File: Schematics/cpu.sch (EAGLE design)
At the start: 44 parts, among them IC2 LM555N, IC22 74154N, IC3 LM555N, IC4 7400N, IC5 74LS32N, IC6 ATMEGA328-20P, U1 74HC245N,652, U2 74HC245N,652, U3 74HC245N,652, U4 74HC04N,652

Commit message: removed arduino, added io interrupt, finished io read
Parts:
- removed I/O10, I/O11, I/O12, I/O13, I/O14, I/O15, I/O16, I/O2, I/O3, I/O4, I/O5, I/O6, I/O7, I/O8, I/O9: 74AS573N, 74xx-us:74AS573N
- removed IC22: 74154N, 74xx-us:74154N
- added I/O17, I/O18, I/O19, I/O20, I/O21, I/O22, I/O23, I/O24, I/O25, I/O26, I/O27, I/O28, I/O29, I/O30, I/O31, I/O32: 74AS573N, 74xx-us:74AS573N
- added IC7: 74LS32N, 74xx-us:74LS32N
- added IC8, IC9: 74154N, 74xx-us:74154N
- IC6: value ATMEGA328-20P -> 74LS32N; device atmega328:ATMEGA328-20P -> 74xx-us:74LS32N
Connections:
- removed net N$40: I/O3A.OC, IC22A.2
- removed net N$41: I/O4A.OC, IC22A.3
- removed net N$42: I/O5A.OC, IC22A.4
- removed net N$43: I/O6A.OC, IC22A.5
- removed net N$44: I/O7A.OC, IC22A.6
- removed net N$45: I/O8A.OC, IC22A.7
- removed net N$46: I/O9A.OC, IC22A.8
- removed net N$47: I/O10A.OC, IC22A.9
- removed net N$48: I/O11A.OC, IC22A.10
- removed net N$49: I/O12A.OC, IC22A.11
- removed net N$50: I/O13A.OC, IC22A.12
- removed net N$51: I/O15A.OC, IC22A.13
- removed net N$52: I/O16A.OC, IC22A.14
- removed net N$53: IC6.(PCI18/INT0)PD2
- removed net N$54: IC6.(PCI19/INT1/OC2B)PD3
- removed net N$55: IC6.(PCI12/ADC4/SDA)PC4
- removed net N$56: IC6.(PCI13/ADC5/SCL)PC5
- removed net N$57: IC6.(PCI16/RXD)PD0
- removed net N$58: IC6.(PCI17/TXD)PD1
- removed net N$59: IC6.(PCI5/SCK)PB5
- removed net N$60: IC6.(PCI4/MISO)PB4
- removed net N$61: IC6.(PCI3/MOSI/OC2A)PB3
- removed net N$62: IC6.(PCI2/SS/OC1B)PB2
- removed net N$63: IC6.(PCI21/T1/OC0B)PD5
- new net IOADD0: IC9A.A
- new net IOADD1: IC9A.B
- new net IOADD2: IC9A.C
- new net IOADD3: IC9A.D
- new net IO_READ_CPULS0: I/O17A.OC, IC8A.0
- new net IO_READ_CPULS1: I/O18A.OC, IC8A.1
- new net IO_READ_CPULS10: I/O27A.OC, IC8A.10
- new net IO_READ_CPULS11: I/O28A.OC, IC8A.11
- new net IO_READ_CPULS12: I/O29A.OC, IC8A.12
- new net IO_READ_CPULS13: I/O30A.OC, IC8A.13
- new net IO_READ_CPULS14: I/O31A.OC, IC8A.14
- new net IO_READ_CPULS15: I/O32A.OC, IC8A.15
- new net IO_READ_CPULS2: I/O19A.OC, IC8A.2
- new net IO_READ_CPULS3: I/O20A.OC, IC8A.3
- new net IO_READ_CPULS4: I/O21A.OC, IC8A.4
- new net IO_READ_CPULS5: I/O22A.OC, IC8A.5
- new net IO_READ_CPULS6: I/O23A.OC, IC8A.6
- new net IO_READ_CPULS7: I/O24A.OC, IC8A.7
- new net IO_READ_CPULS8: I/O25A.OC, IC8A.8
- new net IO_READ_CPULS9: I/O26A.OC, IC8A.9
- new net IO_READ_IOLS0: I/O17A.C, IC9A.0
- new net IO_READ_IOLS1: I/O18A.C, IC9A.1
- new net IO_READ_IOLS10: I/O27A.C, IC9A.10
- new net IO_READ_IOLS11: I/O28A.C, IC9A.11
- new net IO_READ_IOLS12: I/O29A.C, IC9A.12
- new net IO_READ_IOLS13: I/O30A.C, IC9A.13
- new net IO_READ_IOLS14: I/O31A.C, IC9A.14
- new net IO_READ_IOLS15: I/O32A.C, IC9A.15
- new net IO_READ_IOLS2: I/O19A.C, IC9A.2
- new net IO_READ_IOLS3: I/O20A.C, IC9A.3
- new net IO_READ_IOLS4: I/O21A.C, IC9A.4
- new net IO_READ_IOLS5: I/O22A.C, IC9A.5
- new net IO_READ_IOLS6: I/O23A.C, IC9A.6
- new net IO_READ_IOLS7: I/O24A.C, IC9A.7
- new net IO_READ_IOLS8: I/O25A.C, IC9A.8
- new net IO_READ_IOLS9: I/O26A.C, IC9A.9
- new net LATCH_EN: IC9A.G1, IC9A.G2
- new net M1: IC7D.I1
- net ADD0: now also IC8A.A; no longer IC22A.A
- net ADD1: now also IC8A.B; no longer IC22A.B
- net ADD2: now also IC8A.C; no longer IC22A.C
- net ADD3: now also IC8A.D; no longer IC22A.D
- net DAT0: now also I/O17A.1Q, I/O18A.1Q, I/O19A.1Q, I/O20A.1Q, I/O21A.1Q, I/O22A.1Q, I/O23A.1Q, I/O24A.1Q, I/O25A.1Q, I/O26A.1Q, I/O27A.1Q, I/O28A.1Q, I/O29A.1Q, I/O30A.1Q, I/O31A.1Q, I/O32A.1Q; no longer I/O10A.1Q, I/O11A.1Q, I/O12A.1Q, I/O13A.1Q, I/O14A.1Q, I/O15A.1Q, I/O16A.1Q, I/O2A.1Q, I/O3A.1Q, I/O4A.1Q, I/O5A.1Q, I/O6A.1Q, I/O7A.1Q, I/O8A.1Q, I/O9A.1Q
- net DAT1: now also I/O17A.2Q, I/O18A.2Q, I/O19A.2Q, I/O20A.2Q, I/O21A.2Q, I/O22A.2Q, I/O23A.2Q, I/O24A.2Q, I/O25A.2Q, I/O26A.2Q, I/O27A.2Q, I/O28A.2Q, I/O29A.2Q, I/O30A.2Q, I/O31A.2Q, I/O32A.2Q; no longer I/O10A.2Q, I/O11A.2Q, I/O12A.2Q, I/O13A.2Q, I/O14A.2Q, I/O15A.2Q, I/O16A.2Q, I/O2A.2Q, I/O3A.2Q, I/O4A.2Q, I/O5A.2Q, I/O6A.2Q, I/O7A.2Q, I/O8A.2Q, I/O9A.2Q
- net DAT2: now also I/O17A.3Q, I/O18A.3Q, I/O19A.3Q, I/O20A.3Q, I/O21A.3Q, I/O22A.3Q, I/O23A.3Q, I/O24A.3Q, I/O25A.3Q, I/O26A.3Q, I/O27A.3Q, I/O28A.3Q, I/O29A.3Q, I/O30A.3Q, I/O31A.3Q, I/O32A.3Q; no longer I/O10A.3Q, I/O11A.3Q, I/O12A.3Q, I/O13A.3Q, I/O14A.3Q, I/O15A.3Q, I/O16A.3Q, I/O2A.3Q, I/O3A.3Q, I/O4A.3Q, I/O5A.3Q, I/O6A.3Q, I/O7A.3Q, I/O8A.3Q, I/O9A.3Q
- net DAT3: now also I/O17A.4Q, I/O18A.4Q, I/O19A.4Q, I/O20A.4Q, I/O21A.4Q, I/O22A.4Q, I/O23A.4Q, I/O24A.4Q, I/O25A.4Q, I/O26A.4Q, I/O27A.4Q, I/O28A.4Q, I/O29A.4Q, I/O30A.4Q, I/O31A.4Q, I/O32A.4Q; no longer I/O10A.4Q, I/O11A.4Q, I/O12A.4Q, I/O13A.4Q, I/O14A.4Q, I/O15A.4Q, I/O16A.4Q, I/O2A.4Q, I/O3A.4Q, I/O4A.4Q, I/O5A.4Q, I/O6A.4Q, I/O7A.4Q, I/O8A.4Q, I/O9A.4Q
- net DAT4: now also I/O17A.5Q, I/O18A.5Q, I/O19A.5Q, I/O20A.5Q, I/O21A.5Q, I/O22A.5Q, I/O23A.5Q, I/O24A.5Q, I/O25A.5Q, I/O26A.5Q, I/O27A.5Q, I/O28A.5Q, I/O29A.5Q, I/O30A.5Q, I/O31A.5Q, I/O32A.5Q; no longer I/O10A.5Q, I/O11A.5Q, I/O12A.5Q, I/O13A.5Q, I/O14A.5Q, I/O15A.5Q, I/O16A.5Q, I/O2A.5Q, I/O3A.5Q, I/O4A.5Q, I/O5A.5Q, I/O6A.5Q, I/O7A.5Q, I/O8A.5Q, I/O9A.5Q
- net DAT5: now also I/O17A.6Q, I/O18A.6Q, I/O19A.6Q, I/O20A.6Q, I/O21A.6Q, I/O22A.6Q, I/O23A.6Q, I/O24A.6Q, I/O25A.6Q, I/O26A.6Q, I/O27A.6Q, I/O28A.6Q, I/O29A.6Q, I/O30A.6Q, I/O31A.6Q, I/O32A.6Q; no longer I/O10A.6Q, I/O11A.6Q, I/O12A.6Q, I/O13A.6Q, I/O14A.6Q, I/O15A.6Q, I/O16A.6Q, I/O2A.6Q, I/O3A.6Q, I/O4A.6Q, I/O5A.6Q, I/O6A.6Q, I/O7A.6Q, I/O8A.6Q, I/O9A.6Q
- net DAT6: now also I/O17A.7Q, I/O18A.7Q, I/O19A.7Q, I/O20A.7Q, I/O21A.7Q, I/O22A.7Q, I/O23A.7Q, I/O24A.7Q, I/O25A.7Q, I/O26A.7Q, I/O27A.7Q, I/O28A.7Q, I/O29A.7Q, I/O30A.7Q, I/O31A.7Q, I/O32A.7Q; no longer I/O10A.7Q, I/O11A.7Q, I/O12A.7Q, I/O13A.7Q, I/O14A.7Q, I/O15A.7Q, I/O16A.7Q, I/O2A.7Q, I/O3A.7Q, I/O4A.7Q, I/O5A.7Q, I/O6A.7Q, I/O7A.7Q, I/O8A.7Q, I/O9A.7Q
- net DAT7: now also I/O17A.8Q, I/O18A.8Q, I/O19A.8Q, I/O20A.8Q, I/O21A.8Q, I/O22A.8Q, I/O23A.8Q, I/O24A.8Q, I/O25A.8Q, I/O26A.8Q, I/O27A.8Q, I/O28A.8Q, I/O29A.8Q, I/O30A.8Q, I/O31A.8Q, I/O32A.8Q; no longer I/O10A.8Q, I/O11A.8Q, I/O12A.8Q, I/O13A.8Q, I/O14A.8Q, I/O15A.8Q, I/O16A.8Q, I/O2A.8Q, I/O3A.8Q, I/O4A.8Q, I/O5A.8Q, I/O6A.8Q, I/O7A.8Q, I/O8A.8Q, I/O9A.8Q
- net I/ODAT0: now also I/O17A.1D, I/O19A.1D, I/O20A.1D, I/O21A.1D, I/O22A.1D, I/O23A.1D, I/O24A.1D, I/O25A.1D, I/O26A.1D, I/O27A.1D, I/O28A.1D, I/O29A.1D, I/O30A.1D, I/O31A.1D, I/O32A.1D; no longer I/O10A.1D, I/O11A.1D, I/O12A.1D, I/O13A.1D, I/O14A.1D, I/O15A.1D, I/O16A.1D, I/O3A.1D, I/O4A.1D, I/O5A.1D, I/O6A.1D, I/O7A.1D, I/O8A.1D, I/O9A.1D
- net I/ODAT1: now also I/O17A.2D, I/O19A.2D, I/O20A.2D, I/O21A.2D, I/O22A.2D, I/O23A.2D, I/O24A.2D, I/O25A.2D, I/O26A.2D, I/O27A.2D, I/O28A.2D, I/O29A.2D, I/O30A.2D, I/O31A.2D, I/O32A.2D; no longer I/O10A.2D, I/O11A.2D, I/O12A.2D, I/O13A.2D, I/O14A.2D, I/O15A.2D, I/O16A.2D, I/O3A.2D, I/O4A.2D, I/O5A.2D, I/O6A.2D, I/O7A.2D, I/O8A.2D, I/O9A.2D
- net I/ODAT2: now also I/O17A.3D, I/O19A.3D, I/O20A.3D, I/O21A.3D, I/O22A.3D, I/O23A.3D, I/O24A.3D, I/O25A.3D, I/O26A.3D, I/O27A.3D, I/O28A.3D, I/O29A.3D, I/O30A.3D, I/O31A.3D, I/O32A.3D; no longer I/O10A.3D, I/O11A.3D, I/O12A.3D, I/O13A.3D, I/O14A.3D, I/O15A.3D, I/O16A.3D, I/O3A.3D, I/O4A.3D, I/O5A.3D, I/O6A.3D, I/O7A.3D, I/O8A.3D, I/O9A.3D
- net I/ODAT3: now also I/O17A.4D, I/O19A.4D, I/O20A.4D, I/O21A.4D, I/O22A.4D, I/O23A.4D, I/O24A.4D, I/O25A.4D, I/O26A.4D, I/O27A.4D, I/O28A.4D, I/O29A.4D, I/O30A.4D, I/O31A.4D, I/O32A.4D; no longer I/O10A.4D, I/O11A.4D, I/O12A.4D, I/O13A.4D, I/O14A.4D, I/O15A.4D, I/O16A.4D, I/O3A.4D, I/O4A.4D, I/O5A.4D, I/O6A.4D, I/O7A.4D, I/O8A.4D, I/O9A.4D
- net I/ODAT4: now also I/O17A.5D, I/O19A.5D, I/O20A.5D, I/O21A.5D, I/O22A.5D, I/O23A.5D, I/O24A.5D, I/O25A.5D, I/O26A.5D, I/O27A.5D, I/O28A.5D, I/O29A.5D, I/O30A.5D, I/O31A.5D, I/O32A.5D; no longer I/O10A.5D, I/O11A.5D, I/O12A.5D, I/O13A.5D, I/O14A.5D, I/O15A.5D, I/O16A.5D, I/O3A.5D, I/O4A.5D, I/O5A.5D, I/O6A.5D, I/O7A.5D, I/O8A.5D, I/O9A.5D
- net I/ODAT5: now also I/O17A.6D, I/O19A.6D, I/O20A.6D, I/O21A.6D, I/O22A.6D, I/O23A.6D, I/O24A.6D, I/O25A.6D, I/O26A.6D, I/O27A.6D, I/O28A.6D, I/O29A.6D, I/O30A.6D, I/O31A.6D, I/O32A.6D; no longer I/O10A.6D, I/O11A.6D, I/O12A.6D, I/O13A.6D, I/O14A.6D, I/O15A.6D, I/O16A.6D, I/O3A.6D, I/O4A.6D, I/O5A.6D, I/O6A.6D, I/O7A.6D, I/O8A.6D, I/O9A.6D
- net I/ODAT6: now also I/O17A.7D, I/O19A.7D, I/O20A.7D, I/O21A.7D, I/O22A.7D, I/O23A.7D, I/O24A.7D, I/O25A.7D, I/O26A.7D, I/O27A.7D, I/O28A.7D, I/O29A.7D, I/O30A.7D, I/O31A.7D, I/O32A.7D; no longer I/O10A.7D, I/O11A.7D, I/O12A.7D, I/O13A.7D, I/O14A.7D, I/O15A.7D, I/O16A.7D, I/O3A.7D, I/O4A.7D, I/O5A.7D, I/O6A.7D, I/O7A.7D, I/O8A.7D, I/O9A.7D
- net I/ODAT7: now also I/O17A.8D, I/O19A.8D, I/O20A.8D, I/O21A.8D, I/O22A.8D, I/O23A.8D, I/O24A.8D, I/O25A.8D, I/O26A.8D, I/O27A.8D, I/O28A.8D, I/O29A.8D, I/O30A.8D, I/O31A.8D, I/O32A.8D; no longer I/O10A.8D, I/O11A.8D, I/O12A.8D, I/O13A.8D, I/O14A.8D, I/O15A.8D, I/O16A.8D, I/O3A.8D, I/O4A.8D, I/O5A.8D, I/O6A.8D, I/O7A.8D, I/O8A.8D, I/O9A.8D
- net IORD: now also IC6D.O, IC8A.G1, IC8A.G2; no longer IC22A.G1, IC22A.G2, IC5D.O
- net IORQ: now also IC6D.I1, IC7D.I0; no longer IC5D.I1
- net N$38: now also IC7D.O; no longer IC22A.0
- net N$39: now also I/O1A.C; no longer I/O2A.OC, IC22A.1
- net RD: now also IC6D.I0; no longer IC5D.I0
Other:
- note added: "IO Inturrupt"
- note added: "IO Read"

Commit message: finished io decoding, started to change the latch part used to a better library one
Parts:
- removed I/O1: 74AS573N, 74xx-us:74AS573N
- added IC10: 74LS32N, 74xx-us:74LS32N
- added U5, U6, U7: 74HC373N,652, NXP_By_element14_Batch_1:74HC373N,652
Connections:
- new net 5V: U7.VCC
- new net HALT: IC1.HALT
- new net IORW: IC10D.I0
- new net IO_ADD0: U5.D0
- new net IO_ADD1: U5.D1
- new net IO_ADD2: U5.D2
- new net IO_ADD3: U5.D3
- new net IO_ADD4: U5.D4
- new net IO_ADD5: U5.D5
- new net IO_ADD6: U5.D6
- new net IO_ADD7: U5.D7
- new net IO_INT: U7.LE
- new net N$40: U5.~OE, U6.~OE
- new net RFSH: IC1.RFSH
- new net WAIT: IC1.WAIT
- net ADD0: now also U5.Q0
- net ADD1: now also U5.Q1
- net ADD2: now also U5.Q2
- net ADD3: now also U5.Q3
- net ADD4: now also U5.Q4
- net ADD5: now also U5.Q5
- net ADD6: now also U5.Q6
- net ADD7: now also U5.Q7
- net DAT0: now also U6.Q0, U7.Q0; no longer I/O1A.1Q
- net DAT1: now also U6.Q1, U7.Q1; no longer I/O1A.2Q
- net DAT2: now also U6.Q2, U7.Q2; no longer I/O1A.3Q
- net DAT3: now also U6.Q3, U7.Q3; no longer I/O1A.4Q
- net DAT4: now also U6.Q4, U7.Q4; no longer I/O1A.5Q
- net DAT5: now also U6.Q5, U7.Q5; no longer I/O1A.6Q
- net DAT6: now also U6.Q6, U7.Q6; no longer I/O1A.7Q
- net DAT7: now also U6.Q7, U7.Q7; no longer I/O1A.8Q
- net GND: now also U5.GND, U6.GND, U7.GND
- net I/ODAT0: now also U6.D0, U7.D0; no longer I/O1A.1D
- net I/ODAT1: now also U6.D1, U7.D1; no longer I/O1A.2D
- net I/ODAT2: now also U6.D2, U7.D2; no longer I/O1A.3D
- net I/ODAT3: now also U6.D3, U7.D3; no longer I/O1A.4D
- net I/ODAT4: now also U6.D4, U7.D4; no longer I/O1A.5D
- net I/ODAT5: now also U6.D5, U7.D5; no longer I/O1A.6D
- net I/ODAT6: now also U6.D6, U7.D6; no longer I/O1A.7D
- net I/ODAT7: now also U6.D7, U7.D7; no longer I/O1A.8D
- net N$38: now also U7.~OE; no longer I/O1A.OC
- net N$39: now also IC10D.O, U5.LE, U6.LE; no longer I/O1A.C
- net VCC: now also U5.VCC, U6.VCC
- net WR: now also IC10D.I1
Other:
- note added: "IO Port Write"
- note added: "NOTE: Only utilizing 8 ports of IO read, but all 256 ports of IO write. Maybe the IO controller will do sound as well?"
- moved on the sheet: IC7D

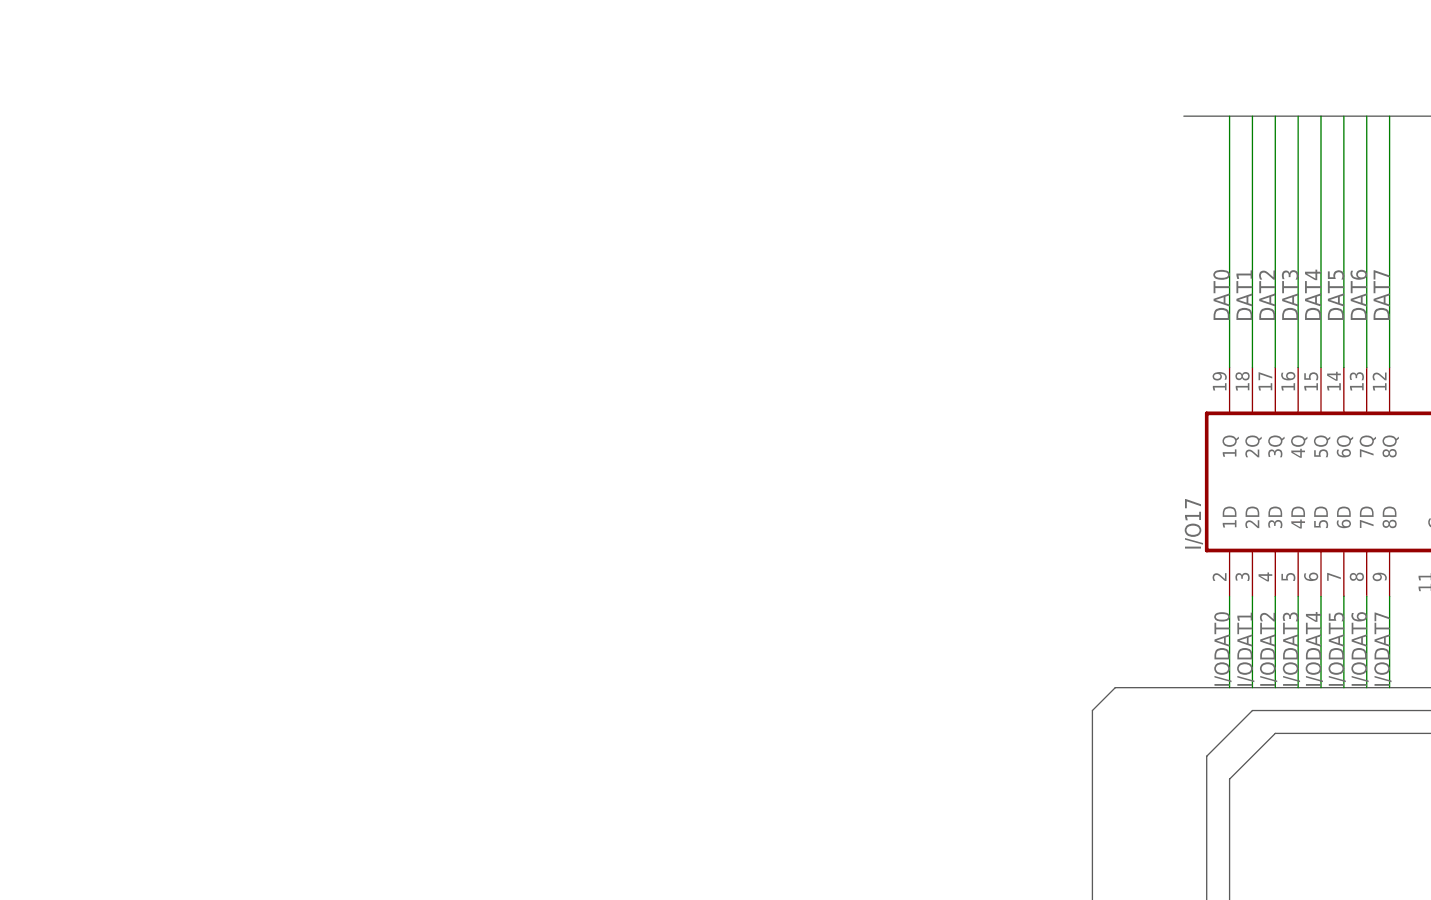
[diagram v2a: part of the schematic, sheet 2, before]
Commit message: figured out 40 pin mapping, started selecting microcontroller
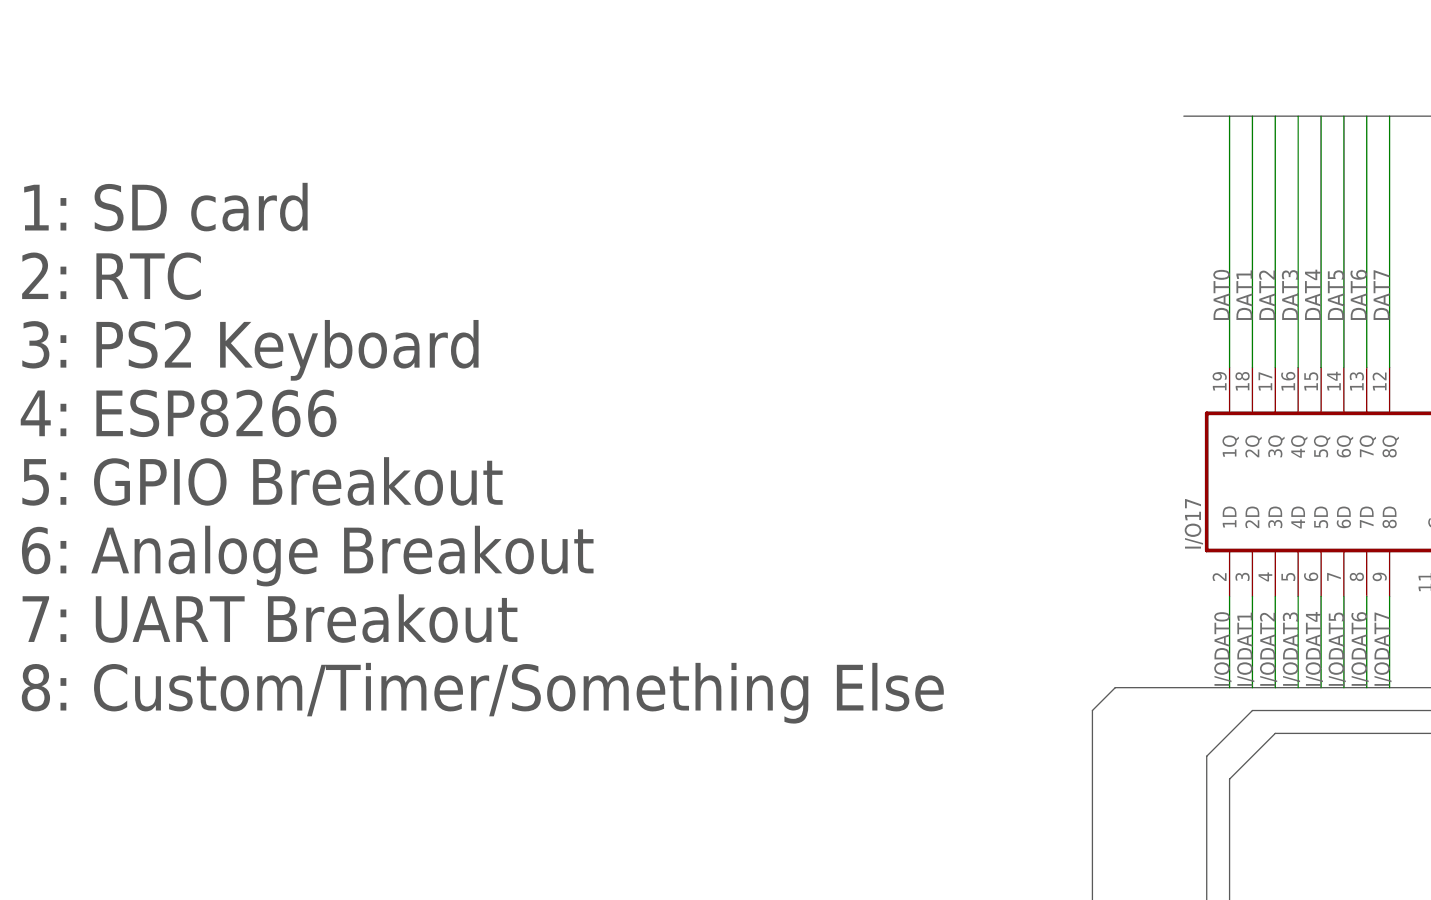
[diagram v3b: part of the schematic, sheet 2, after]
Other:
- note added: "1: SD card 2: RTC 3: PS2 Keyboard 4: ESP8266 5: GPIO Breakout 6: Analoge Breakout 7: UART Breakout 8: Custom/Timer/Something Else"
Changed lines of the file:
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@@
 all 256 ports of IO write. Maybe the IO controller
 will do sound as well?</text>
+<text x="-462.28" y="93.98" size="5.08" layer="97">1: SD card
+2: RTC
+3: PS2 Keyboard
+4: ESP8266
+5: GPIO Breakout
+6: Analoge Breakout
+7: UART Breakout
+8: Custom/Timer/Something Else
+</text>
 </plain>
 <instances>

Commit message: changed latches
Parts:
- removed I/O17, I/O18, I/O19, I/O20, I/O21, I/O22, I/O23, I/O24, I/O25, I/O26, I/O27, I/O28, I/O29, I/O30, I/O31, I/O32: 74AS573N, 74xx-us:74AS573N
- added U10, U11, U12, U13, U14, U15, U8, U9: 74HC373N,652, NXP_By_element14_Batch_1:74HC373N,652
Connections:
- net DAT0: now also U10.Q0, U11.Q0, U12.Q0, U13.Q0, U14.Q0, U15.Q0, U8.Q0, U9.Q0; no longer I/O17A.1Q, I/O18A.1Q, I/O19A.1Q, I/O20A.1Q, I/O21A.1Q, I/O22A.1Q, I/O23A.1Q, I/O24A.1Q, I/O25A.1Q, I/O26A.1Q, I/O27A.1Q, I/O28A.1Q, I/O29A.1Q, I/O30A.1Q, I/O31A.1Q, I/O32A.1Q
- net DAT1: now also U10.Q1, U11.Q1, U12.Q1, U13.Q1, U14.Q1, U15.Q1, U8.Q1, U9.Q1; no longer I/O17A.2Q, I/O18A.2Q, I/O19A.2Q, I/O20A.2Q, I/O21A.2Q, I/O22A.2Q, I/O23A.2Q, I/O24A.2Q, I/O25A.2Q, I/O26A.2Q, I/O27A.2Q, I/O28A.2Q, I/O29A.2Q, I/O30A.2Q, I/O31A.2Q, I/O32A.2Q
- net DAT2: now also U10.Q2, U11.Q2, U12.Q2, U13.Q2, U14.Q2, U15.Q2, U8.Q2, U9.Q2; no longer I/O17A.3Q, I/O18A.3Q, I/O19A.3Q, I/O20A.3Q, I/O21A.3Q, I/O22A.3Q, I/O23A.3Q, I/O24A.3Q, I/O25A.3Q, I/O26A.3Q, I/O27A.3Q, I/O28A.3Q, I/O29A.3Q, I/O30A.3Q, I/O31A.3Q, I/O32A.3Q
- net DAT3: now also U10.Q3, U11.Q3, U12.Q3, U13.Q3, U14.Q3, U15.Q3, U8.Q3, U9.Q3; no longer I/O17A.4Q, I/O18A.4Q, I/O19A.4Q, I/O20A.4Q, I/O21A.4Q, I/O22A.4Q, I/O23A.4Q, I/O24A.4Q, I/O25A.4Q, I/O26A.4Q, I/O27A.4Q, I/O28A.4Q, I/O29A.4Q, I/O30A.4Q, I/O31A.4Q, I/O32A.4Q
- net DAT4: now also U10.Q4, U11.Q4, U12.Q4, U13.Q4, U14.Q4, U15.Q4, U8.Q4, U9.Q4; no longer I/O17A.5Q, I/O18A.5Q, I/O19A.5Q, I/O20A.5Q, I/O21A.5Q, I/O22A.5Q, I/O23A.5Q, I/O24A.5Q, I/O25A.5Q, I/O26A.5Q, I/O27A.5Q, I/O28A.5Q, I/O29A.5Q, I/O30A.5Q, I/O31A.5Q, I/O32A.5Q
- net DAT5: now also U10.Q5, U11.Q5, U12.Q5, U13.Q5, U14.Q5, U15.Q5, U8.Q5, U9.Q5; no longer I/O17A.6Q, I/O18A.6Q, I/O19A.6Q, I/O20A.6Q, I/O21A.6Q, I/O22A.6Q, I/O23A.6Q, I/O24A.6Q, I/O25A.6Q, I/O26A.6Q, I/O27A.6Q, I/O28A.6Q, I/O29A.6Q, I/O30A.6Q, I/O31A.6Q, I/O32A.6Q
- net DAT6: now also U10.Q6, U11.Q6, U12.Q6, U13.Q6, U14.Q6, U15.Q6, U8.Q6, U9.Q6; no longer I/O17A.7Q, I/O18A.7Q, I/O19A.7Q, I/O20A.7Q, I/O21A.7Q, I/O22A.7Q, I/O23A.7Q, I/O24A.7Q, I/O25A.7Q, I/O26A.7Q, I/O27A.7Q, I/O28A.7Q, I/O29A.7Q, I/O30A.7Q, I/O31A.7Q, I/O32A.7Q
- net DAT7: now also U10.Q7, U11.Q7, U12.Q7, U13.Q7, U14.Q7, U15.Q7, U8.Q7, U9.Q7; no longer I/O17A.8Q, I/O18A.8Q, I/O19A.8Q, I/O20A.8Q, I/O21A.8Q, I/O22A.8Q, I/O23A.8Q, I/O24A.8Q, I/O25A.8Q, I/O26A.8Q, I/O27A.8Q, I/O28A.8Q, I/O29A.8Q, I/O30A.8Q, I/O31A.8Q, I/O32A.8Q
- net GND: now also U8.GND
- net I/ODAT0: now also U10.D0, U11.D0, U12.D0, U13.D0, U14.D0, U15.D0, U8.D0, U9.D0; no longer I/O17A.1D, I/O19A.1D, I/O20A.1D, I/O21A.1D, I/O22A.1D, I/O23A.1D, I/O24A.1D, I/O25A.1D, I/O26A.1D, I/O27A.1D, I/O28A.1D, I/O29A.1D, I/O30A.1D, I/O31A.1D, I/O32A.1D
- net I/ODAT1: now also U10.D1, U11.D1, U12.D1, U13.D1, U14.D1, U15.D1, U8.D1, U9.D1; no longer I/O17A.2D, I/O19A.2D, I/O20A.2D, I/O21A.2D, I/O22A.2D, I/O23A.2D, I/O24A.2D, I/O25A.2D, I/O26A.2D, I/O27A.2D, I/O28A.2D, I/O29A.2D, I/O30A.2D, I/O31A.2D, I/O32A.2D
- net I/ODAT2: now also U10.D2, U11.D2, U12.D2, U13.D2, U14.D2, U15.D2, U8.D2, U9.D2; no longer I/O17A.3D, I/O19A.3D, I/O20A.3D, I/O21A.3D, I/O22A.3D, I/O23A.3D, I/O24A.3D, I/O25A.3D, I/O26A.3D, I/O27A.3D, I/O28A.3D, I/O29A.3D, I/O30A.3D, I/O31A.3D, I/O32A.3D
- net I/ODAT3: now also U10.D3, U11.D3, U12.D3, U13.D3, U14.D3, U15.D3, U8.D3, U9.D3; no longer I/O17A.4D, I/O19A.4D, I/O20A.4D, I/O21A.4D, I/O22A.4D, I/O23A.4D, I/O24A.4D, I/O25A.4D, I/O26A.4D, I/O27A.4D, I/O28A.4D, I/O29A.4D, I/O30A.4D, I/O31A.4D, I/O32A.4D
- net I/ODAT4: now also U10.D4, U11.D4, U12.D4, U13.D4, U14.D4, U15.D4, U8.D4, U9.D4; no longer I/O17A.5D, I/O19A.5D, I/O20A.5D, I/O21A.5D, I/O22A.5D, I/O23A.5D, I/O24A.5D, I/O25A.5D, I/O26A.5D, I/O27A.5D, I/O28A.5D, I/O29A.5D, I/O30A.5D, I/O31A.5D, I/O32A.5D
- net I/ODAT5: now also U10.D5, U11.D5, U12.D5, U13.D5, U14.D5, U15.D5, U8.D5, U9.D5; no longer I/O17A.6D, I/O19A.6D, I/O20A.6D, I/O21A.6D, I/O22A.6D, I/O23A.6D, I/O24A.6D, I/O25A.6D, I/O26A.6D, I/O27A.6D, I/O28A.6D, I/O29A.6D, I/O30A.6D, I/O31A.6D, I/O32A.6D
- net I/ODAT6: now also U10.D6, U11.D6, U12.D6, U13.D6, U14.D6, U15.D6, U8.D6, U9.D6; no longer I/O17A.7D, I/O19A.7D, I/O20A.7D, I/O21A.7D, I/O22A.7D, I/O23A.7D, I/O24A.7D, I/O25A.7D, I/O26A.7D, I/O27A.7D, I/O28A.7D, I/O29A.7D, I/O30A.7D, I/O31A.7D, I/O32A.7D
- net I/ODAT7: now also U10.D7, U11.D7, U12.D7, U13.D7, U14.D7, U15.D7, U8.D7, U9.D7; no longer I/O17A.8D, I/O19A.8D, I/O20A.8D, I/O21A.8D, I/O22A.8D, I/O23A.8D, I/O24A.8D, I/O25A.8D, I/O26A.8D, I/O27A.8D, I/O28A.8D, I/O29A.8D, I/O30A.8D, I/O31A.8D, I/O32A.8D
- net IO_READ_CPULS0: now also U8.~OE; no longer I/O17A.OC
- net IO_READ_CPULS1: now also U9.~OE; no longer I/O18A.OC
- net IO_READ_CPULS10: no longer I/O27A.OC
- net IO_READ_CPULS11: no longer I/O28A.OC
- net IO_READ_CPULS12: no longer I/O29A.OC
- net IO_READ_CPULS13: no longer I/O30A.OC
- net IO_READ_CPULS14: no longer I/O31A.OC
- net IO_READ_CPULS15: no longer I/O32A.OC
- net IO_READ_CPULS2: now also U10.~OE; no longer I/O19A.OC
- net IO_READ_CPULS3: now also U11.~OE; no longer I/O20A.OC
- net IO_READ_CPULS4: now also U12.~OE; no longer I/O21A.OC
- net IO_READ_CPULS5: now also U13.~OE; no longer I/O22A.OC
- net IO_READ_CPULS6: now also U14.~OE; no longer I/O23A.OC
- net IO_READ_CPULS7: now also U15.~OE; no longer I/O24A.OC
- net IO_READ_CPULS8: no longer I/O25A.OC
- net IO_READ_CPULS9: no longer I/O26A.OC
- net IO_READ_IOLS0: now also U8.LE; no longer I/O17A.C
- net IO_READ_IOLS1: now also U9.LE; no longer I/O18A.C
- net IO_READ_IOLS10: no longer I/O27A.C
- net IO_READ_IOLS11: no longer I/O28A.C
- net IO_READ_IOLS12: no longer I/O29A.C
- net IO_READ_IOLS13: no longer I/O30A.C
- net IO_READ_IOLS14: no longer I/O31A.C
- net IO_READ_IOLS15: no longer I/O32A.C
- net IO_READ_IOLS2: now also U10.LE; no longer I/O19A.C
- net IO_READ_IOLS3: now also U11.LE; no longer I/O20A.C
- net IO_READ_IOLS4: now also U12.LE; no longer I/O21A.C
- net IO_READ_IOLS5: now also U13.LE; no longer I/O22A.C
- net IO_READ_IOLS6: now also U14.LE; no longer I/O23A.C
- net IO_READ_IOLS7: now also U15.LE; no longer I/O24A.C
- net IO_READ_IOLS8: no longer I/O25A.C
- net IO_READ_IOLS9: no longer I/O26A.C
- net VCC: now also U8.VCC
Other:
- moved on the sheet: IC6D, IC8, IC9
